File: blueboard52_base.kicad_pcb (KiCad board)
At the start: 2 copper layers, 42.2 x 42.5 mm, 19 parts, among them J1 Conn_East, J2 Conn_West, J3 Conn_South, J4 PWR, J5 PWR, J6 NFC, SW1 RST, SW2 DFU, U1 E73-2G4M04S-52832

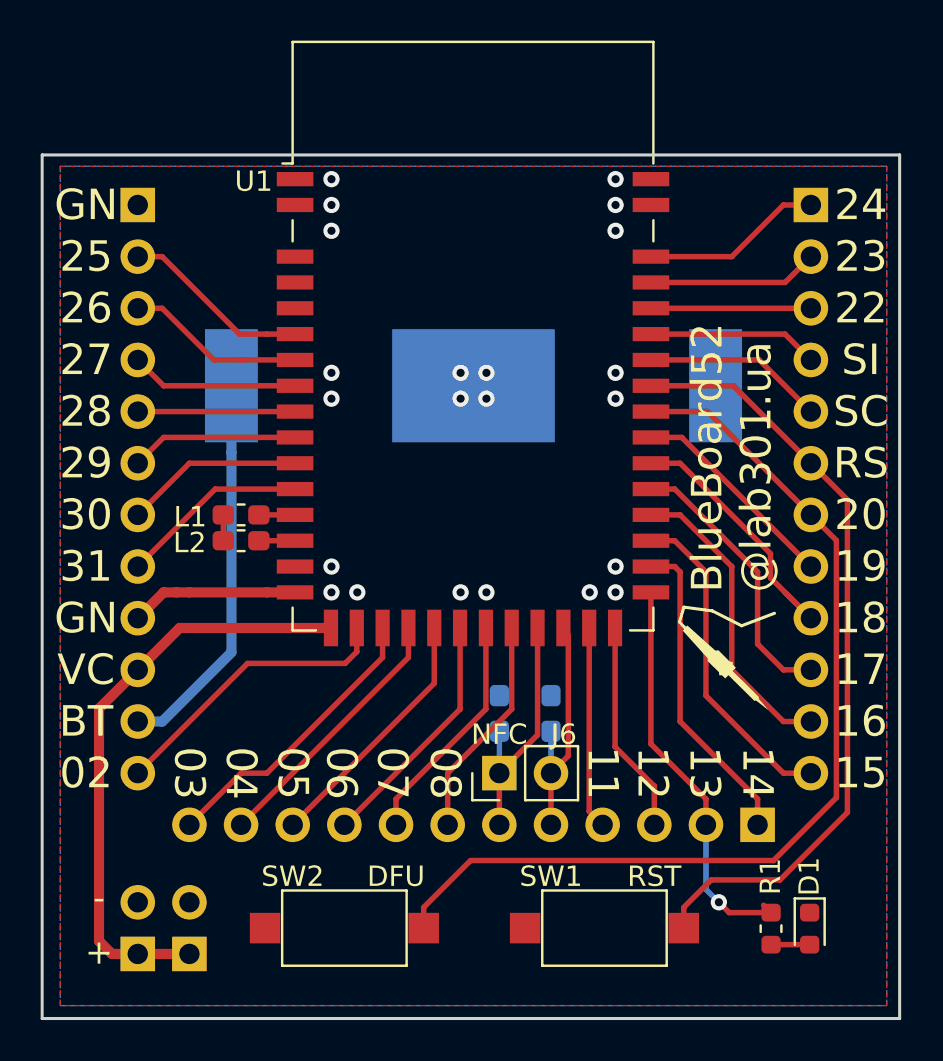
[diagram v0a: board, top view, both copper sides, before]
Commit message: v0.2.3 - Power out connection and dimentions
- Moved power out connector to be friendly with 2.54mm breadboard grid
- Updated annotation for power out connector
- For power **input** you are still supposed to use VC and GN pins
  (it should not matter much, just connections are shorter)
- Updated PCB dimentions: now it's pretty 42x42mm square,
  no fractional dimentsions anymore
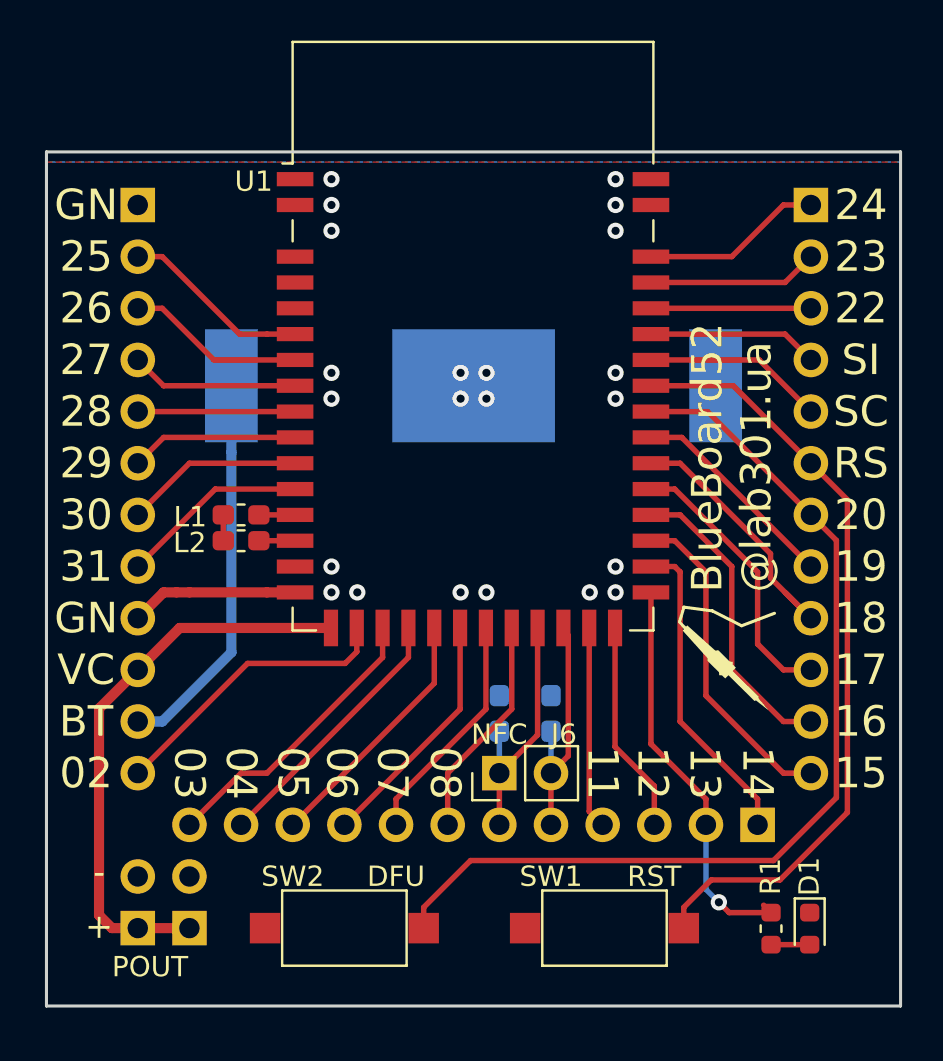
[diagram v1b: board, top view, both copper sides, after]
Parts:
- J4, J5: value PWR -> POUT
- moved J4 1.27 mm to (56.7, 67.1)
- moved J5 1.27 mm to (59.2, 67.1)
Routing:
- net VCC: track 29.2 -> 27.9 mm
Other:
- board size 42.2 x 42.5 mm -> 42 x 42 mm
- board text added: "GN: Ground SI: SWD Data SC: SWD Clock RS: Reset VC: VCC"
- board text added: "POUT"
- board text added: "v0.2.3 git.io/JftkJ"
- board text removed: "GN: Ground SI: SWDIO, Data SC: SWDCLK, Clock RS: Reset VC: VCC"
- board text removed: "v0.2.2 git.io/JvDuP"
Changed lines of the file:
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@@
   (general
     (thickness 1.6)
-    (drawings 84)
+    (drawings 86)
     (tracks 160)
     (zones 0)
@@
   (page A4)
   (layers
-    (0 F.Cu signal hide)
-    (31 B.Cu signal hide)
+    (0 F.Cu signal)
+    (31 B.Cu signal)
     (32 B.Adhes user)
     (33 F.Adhes user)
@@
     (add_net "Net-(L1-Pad2)")
     (add_net "Net-(L2-Pad2)")
-    (add_net "Net-(U1-Pad14)")
-    (add_net "Net-(U1-Pad3)")
-    (add_net "Net-(U1-Pad4)")
   )
   (net_class Power ""
@@
   )
   (module Connector_PinHeader_2.54mm:PinHeader_1x02_P2.54mm_Vertical (layer B.Cu)
-    (at 59.2 68.37)
+    (at 59.2 67.1)
     (descr "Through hole straight pin header, 1x02, 2.54mm pitch, single row")
     (tags "Through hole pin header THT 1x02 2.54mm single row")
-    (fp_text reference J5 (at 0 -5.08 270) (layer B.SilkS)
-      (effects (font (size 1 1) (thickness 0.15)) (justify mirror))
-    )
-    (fp_text value PWR (at -2.54 -1.27 90) (layer B.SilkS)
+    (fp_text reference J5 (at 0 2.54 270) (layer B.SilkS)
+      (effects (font (size 1 1) (thickness 0.15)) (justify mirror))
+    )
+    (fp_text value POUT (at 0 -1.27 90) (layer B.SilkS) hide
       (effects (font (size 1 1) (thickness 0.15)) (justify mirror))
     )
@@
   )
   (module Connector_PinHeader_2.54mm:PinHeader_1x02_P2.54mm_Vertical (layer B.Cu)
-    (at 56.66 68.37)
+    (at 56.66 67.1)
     (descr "Through hole straight pin header, 1x02, 2.54mm pitch, single row")
     (tags "Through hole pin header THT 1x02 2.54mm single row")
-    (fp_text reference J4 (at 0 -5.08 270) (layer B.SilkS)
-      (effects (font (size 1 1) (thickness 0.15)) (justify mirror))
-    )
-    (fp_text value PWR (at 2.54 -1.27 90) (layer B.SilkS)
+    (fp_text reference J4 (at 0 2.54 270) (layer B.SilkS)
+      (effects (font (size 1 1) (thickness 0.15)) (justify mirror))
+    )
+    (fp_text value POUT (at 0 -1.27 90) (layer B.SilkS) hide
       (effects (font (size 1 1) (thickness 0.15)) (justify mirror))
     )
@@
     )
   )
-  (gr_text "GN: Ground\nSI: SWDIO, Data\nSC: SWDCLK, Clock\nRS: Reset\nVC: VCC" (at 88.41 53.13) (layer B.SilkS)
+  (gr_text POUT (at 61.74 63.925 90) (layer B.SilkS)
+    (effects (font (size 1 1) (thickness 0.15)) (justify left mirror))
+  )
+  (gr_text POUT (at 55.39 69.005) (layer F.SilkS)
+    (effects (font (size 1 1) (thickness 0.15)) (justify left))
+  )
+  (gr_line (start 52.17 70.93) (end 94.17 70.93) (layer Edge.Cuts) (width 0.15))
+  (gr_text "GN: Ground\nSI: SWD Data\nSC: SWD Clock\nRS: Reset\nVC: VCC" (at 88.41 53.13) (layer B.SilkS)
     (effects (font (size 1 1) (thickness 0.15)) (justify left mirror))
   )
@@
     (effects (font (size 1.5 1.5) (thickness 0.3)) (justify mirror))
   )
-  (gr_text - (at 54.755 65.83 180) (layer F.SilkS)
+  (gr_text - (at 54.755 64.56 180) (layer F.SilkS)
     (effects (font (size 1.2 1.2) (thickness 0.3)))
   )
-  (gr_text - (at 54.755 65.83 180) (layer B.SilkS)
+  (gr_text - (at 54.755 64.56 180) (layer B.SilkS)
     (effects (font (size 1.2 1.2) (thickness 0.3)) (justify mirror))
   )
-  (gr_text + (at 54.755 68.37 180) (layer B.SilkS)
+  (gr_text + (at 54.755 67.1 180) (layer B.SilkS)
     (effects (font (size 1.2 1.2) (thickness 0.3)) (justify mirror))
   )
@@
     (effects (font (size 1.5 1.5) (thickness 0.3)))
   )
-  (gr_text + (at 54.755 68.37 180) (layer F.SilkS)
+  (gr_text + (at 54.755 67.1 180) (layer F.SilkS)
     (effects (font (size 1.2 1.2) (thickness 0.3)))
   )
@@
     (effects (font (size 1.5 1.5) (thickness 0.3)))
   )
-  (gr_text "v0.2.2\ngit.io/JvDuP" (at 79.52 67.1) (layer B.SilkS)
+  (gr_text "v0.2.3\ngit.io/JftkJ" (at 79.52 67.1) (layer B.SilkS)
     (effects (font (size 1.5 1.5) (thickness 0.3)) (justify left mirror))
   )
@@
     (effects (font (size 1.5 1.5) (thickness 0.3)) (justify left))
   )
-  (gr_line (start 51.96 71.545) (end 94.125 71.545) (layer Edge.Cuts) (width 0.15))
-  (gr_line (start 51.96 29.08) (end 51.96 71.545) (layer Edge.Cuts) (width 0.15))
-  (gr_line (start 94.125 29.08) (end 51.96 29.08) (layer Edge.Cuts) (width 0.15))
-  (gr_line (start 94.125 71.545) (end 94.125 29.08) (layer Edge.Cuts) (width 0.15))
+  (gr_line (start 52.17 28.93) (end 52.17 70.93) (layer Edge.Cuts) (width 0.15))
+  (gr_line (start 94.17 28.93) (end 52.17 28.93) (layer Edge.Cuts) (width 0.15))
+  (gr_line (start 94.17 70.93) (end 94.17 28.93) (layer Edge.Cuts) (width 0.15))
+  (segment (start 64.395 46.78) (end 62.615 46.78) (width 0.27) (layer F.Cu) (net 1))
+  (segment (start 62.615 48.05) (end 64.395 48.05) (width 0.27) (layer F.Cu) (net 2))
+  (segment (start 58.72 52.34) (end 56.66 54.4) (width 0.5) (layer F.Cu) (net 3))
+  (segment (start 66.16 52.34) (end 58.72 52.34) (width 0.5) (layer F.Cu) (net 3))
+  (segment (start 55.39 67.1) (end 56.66 67.1) (width 0.5) (layer F.Cu) (net 3))
+  (segment (start 59.2 67.1) (end 56.66 67.1) (width 0.5) (layer F.Cu) (net 3))
+  (segment (start 56.66 54.4) (end 54.755 56.305) (width 0.5) (layer F.Cu) (net 3))
+  (segment (start 54.755 66.465) (end 55.39 67.1) (width 0.5) (layer F.Cu) (net 3))
+  (segment (start 54.755 56.305) (end 54.755 66.465) (width 0.5) (layer F.Cu) (net 3))
+  (segment (start 60.865 46.78) (end 60.865 48.05) (width 0.27) (layer F.Cu) (net 4))
   (via (at 72.535 41.065) (size 0.8) (drill 0.4) (layers F.Cu B.Cu) (net 5))
   (via (at 73.805 41.065) (size 0.8) (drill 0.4) (layers F.Cu B.Cu) (net 5))
   (via (at 73.805 39.795) (size 0.8) (drill 0.4) (layers F.Cu B.Cu) (net 5))
   (via (at 72.535 39.795) (size 0.8) (drill 0.4) (layers F.Cu B.Cu) (net 5))
-  (segment (start 64.395 46.78) (end 62.615 46.78) (width 0.27) (layer F.Cu) (net 1))
-  (segment (start 62.615 48.05) (end 64.395 48.05) (width 0.27) (layer F.Cu) (net 2))
-  (segment (start 58.72 52.34) (end 56.66 54.4) (width 0.5) (layer F.Cu) (net 3))
-  (segment (start 66.16 52.34) (end 58.72 52.34) (width 0.5) (layer F.Cu) (net 3))
-  (segment (start 60.865 46.78) (end 60.865 48.05) (width 0.27) (layer F.Cu) (net 4))
   (via (at 80.155 41.065) (size 0.8) (drill 0.4) (layers F.Cu B.Cu) (net 5))
   (via (at 66.185 49.32) (size 0.8) (drill 0.4) (layers F.Cu B.Cu) (net 5))
@@
   (via (at 80.155 31.54) (size 0.8) (drill 0.4) (layers F.Cu B.Cu) (net 5))
   (via (at 66.185 31.54) (size 0.8) (drill 0.4) (layers F.Cu B.Cu) (net 5))
-  (segment (start 55.39 68.37) (end 56.66 68.37) (width 0.5) (layer F.Cu) (net 3))
-  (segment (start 59.2 68.37) (end 56.66 68.37) (width 0.5) (layer F.Cu) (net 3))
-  (segment (start 54.755 56.305) (end 54.755 67.735) (width 0.5) (layer F.Cu) (net 3))
-  (segment (start 56.66 54.4) (end 54.755 56.305) (width 0.5) (layer F.Cu) (net 3))
-  (segment (start 54.755 67.735) (end 55.39 68.37) (width 0.5) (layer F.Cu) (net 3))
   (segment (start 59.2 50.59) (end 58.565 50.59) (width 0.5) (layer F.Cu) (net 5))
   (segment (start 63.01 50.59) (end 59.2 50.59) (width 0.5) (layer F.Cu) (net 5))
@@
   (segment (start 67.43 53.51) (end 67.43 52.34) (width 0.27) (layer F.Cu) (net 13))
   (segment (start 66.8575 54.0825) (end 67.43 53.51) (width 0.27) (layer F.Cu) (net 13))
+  (segment (start 56.66 59.48) (end 62.0575 54.0825) (width 0.27) (layer F.Cu) (net 13))
   (segment (start 62.0575 54.0825) (end 66.8575 54.0825) (width 0.27) (layer F.Cu) (net 13))
-  (segment (start 56.66 59.48) (end 62.0575 54.0825) (width 0.27) (layer F.Cu) (net 13))
   (segment (start 61.265 43.71) (end 61.265 40.43) (width 0.5) (layer B.Cu) (net 14))
   (segment (start 61.265 53.537081) (end 61.265 43.71) (width 0.5) (layer B.Cu) (net 14))
@@
     (polygon
       (pts
-        (xy 52.85 29.635) (xy 93.49 29.635) (xy 93.49 70.91) (xy 52.85 70.91)
+        (xy 52.17 29.43) (xy 94.17 29.43) (xy 94.17 70.93) (xy 52.17 70.93)
       )
     )
@@
     (polygon
       (pts
-        (xy 52.85 70.91) (xy 93.49 70.91) (xy 93.49 29.635) (xy 52.85 29.635)
+        (xy 52.17 70.91) (xy 94.17 70.93) (xy 94.17 29.43) (xy 52.17 29.43)
       )
     )
